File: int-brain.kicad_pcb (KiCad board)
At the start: 2 copper layers, 107 x 79.5 mm, 112 parts, among them J1 Top, J10 2MB, J11 1MB, J12 1MA, J13 1MA_ENC, J14 1MB_ENC, J15 2MA_ENC, J16 MPU9250, J17 VBATT_SELECT, J2 Bottom, J3 PWR, J4 PWR, J5 USB_A, J6 2MB_ENC, J7 I2C0, J8 UART0, J9 2MA, SW1 SW_Push, U1 PCA9635, U10 TPS5450DDA, U11 DRV8251ADDAR, U12 INA139, U13 AMS1117-3.3, U2 ESP32-DevKitC, U3 DRV8251ADDAR, U4 INA139, U5 DRV8251ADDAR, U6 INA139, U7 TPS5450DDA, U8 DRV8251ADDAR, U9 INA139

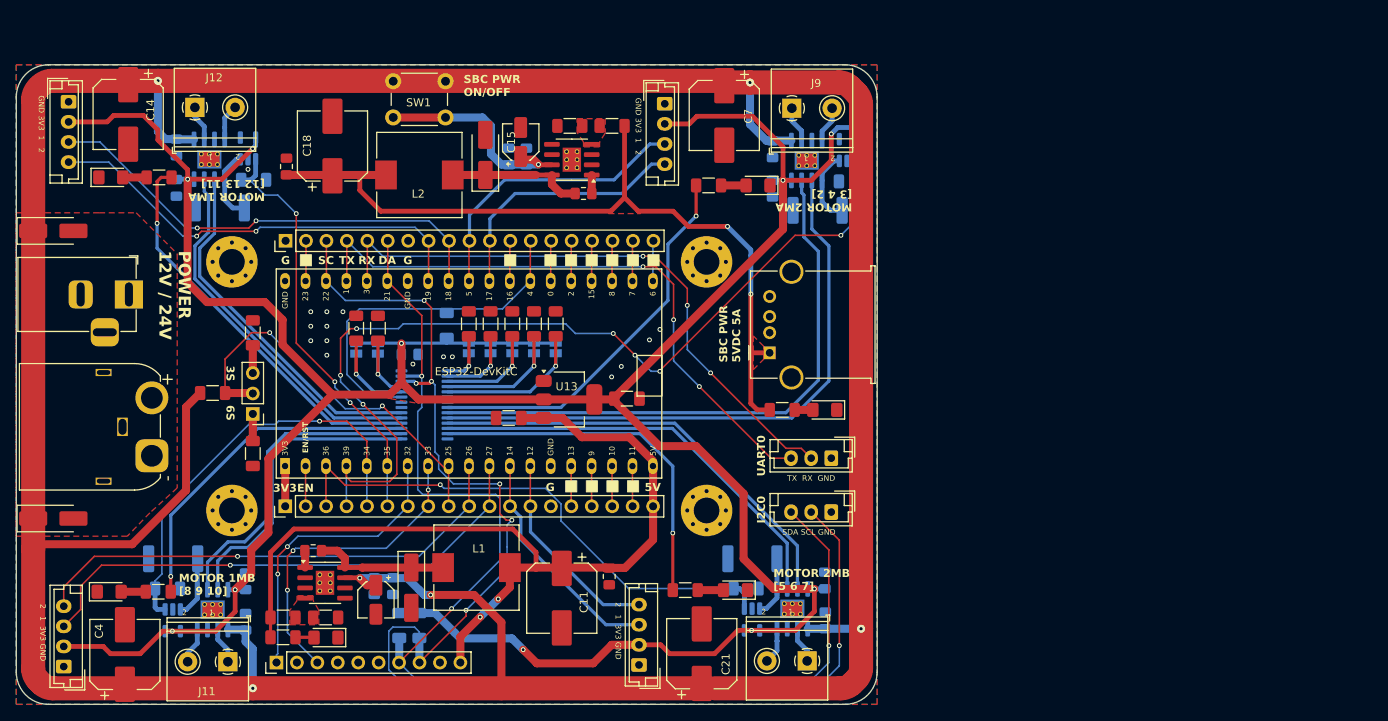
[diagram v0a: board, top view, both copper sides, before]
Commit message: change I2C and minor updates
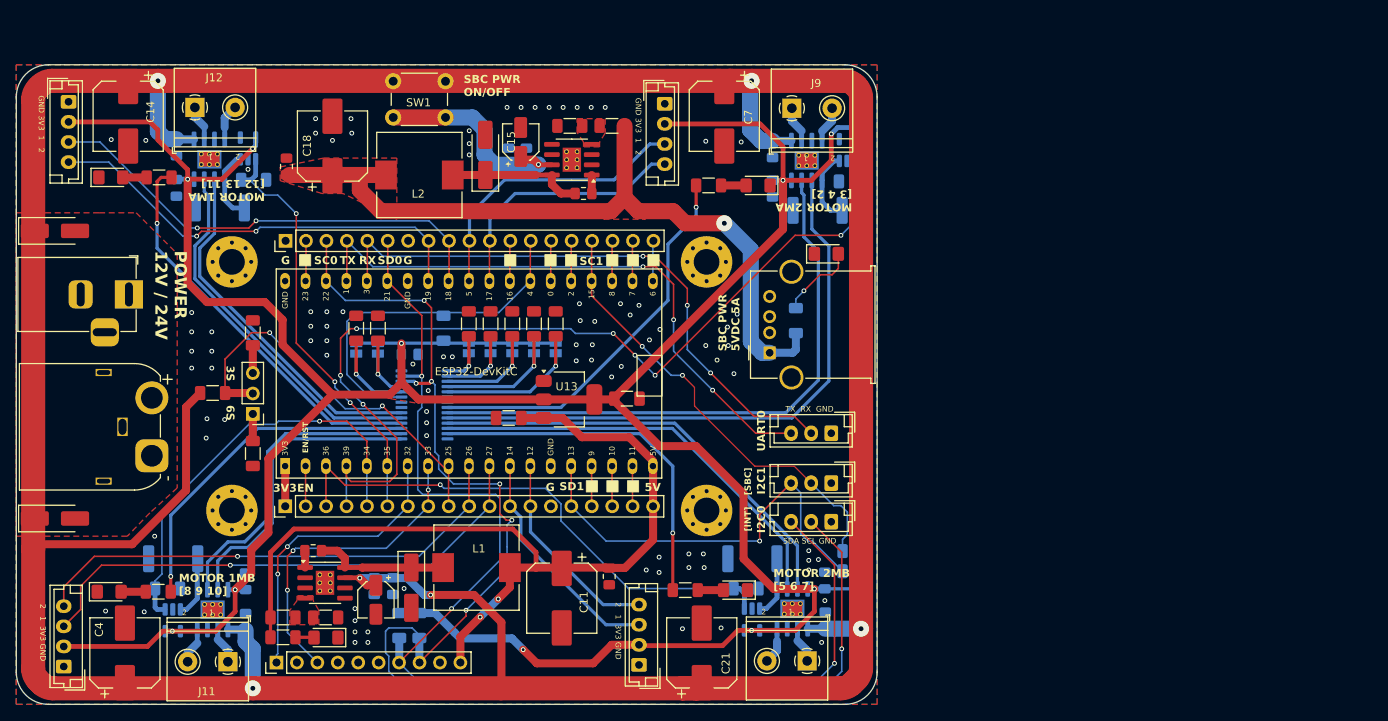
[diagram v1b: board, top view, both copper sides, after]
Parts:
- added J18: I2C0, Connector_JST:JST_EH_B3B-EH-A_1x03_P2.50mm_Vertical, F.Cu at (135.2, 124.5)
- added R32: 4.7k, Resistor_SMD:R_1206_3216Metric_Pad1.30x1.75mm_HandSolder, B.Cu at (138.2, 128.2)
- added R33: 4.7k, Resistor_SMD:R_1206_3216Metric_Pad1.30x1.75mm_HandSolder, B.Cu at (138.2, 130.7)
- J7: value I2C0 -> I2C1
- JP7: value I/O -> A6
- R13: moved to B.Cu
- SW1: value SW_Push -> ON/OFF
- moved D6 19.4 mm to (134.6, 91.2), turned to 0 degrees
- moved R13 11.2 mm to (130.8, 99.5), turned to 90 degrees
- moved J7 3.60 mm to (135.2, 119.7)
- moved J8 3.10 mm to (135.2, 113.5)
- moved R31 0.53 mm to (87.0, 100.5)
- moved C14 0.22 mm to (47.8, 74.1)
- moved D10 0.20 mm to (38.7, 124.1)
- moved D5 0.20 mm to (38.7, 88.3)
- moved C4 0.20 mm to (47.4, 140.8)
- moved C21 0.10 mm to (119.1, 140.8)
- moved C7 0.10 mm to (121.9, 74.1)
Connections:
- net /PCA_IO renamed /PCA_A6
- J1 pad 16: /GPIO15 -> /SCL1
- J2 pad 15: /GPIO13 -> /SDA1
- J7 pad 2: SCL0 -> /SCL1
- J7 pad 3: SDA0 -> /SDA1
- U2 pad 15: /GPIO13 -> /SDA1
- U2 pad 23: /GPIO15 -> /SCL1
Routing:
- net /SCL1: track 0.00 -> 56.2 mm, vias 0 -> 2
- net /SDA1: track 0.00 -> 52.9 mm, vias 0 -> 1
- net /PWR_LED_2: track 2.26 -> 9.81 mm, vias 0 -> 1
- net +3.3V: track 377.3 -> 383.9 mm
- net VS: track 456.3 -> 461.7 mm
- net /GPIO15: track 5.02 -> 0.00 mm
- net /GPIO13: track 5.01 -> 0.00 mm
- net /buck2/VOUT: track 100.2 -> 95.9 mm, vias 2 -> 1
- net /TX0: track 77.0 -> 75.0 mm
- net /RX0: track 75.8 -> 74.6 mm
- net GND: vias 16 -> 91
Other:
- board text added: "SC0"
- board text added: "SC1"
- board text added: "SD0"
- board text added: "SD1"
- board text added: "[INT]"
- board text added: "[SBC]"
- board text removed: "A0"
- board text removed: "A1"
- board text removed: "A2"
- board text removed: "A3"
- board text removed: "A4"
- board text removed: "A5"
- board text removed: "DA"
- board text removed: "I/O"
- board text removed: "SC"

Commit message: done?
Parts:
- JP1, JP2, JP3, JP4, JP5, JP6, JP7, R31: moved to F.Cu
- R11, R12, R14, R29, R4, R6, R7, R9: moved to B.Cu
- moved R14 27.7 mm to (57.7, 112.8), turned to 180 degrees
- moved D7 26.7 mm to (56.1, 117.8), turned to 90 degrees
- moved C26 19.5 mm to (114.6, 112.6), turned to 0 degrees
- moved D6 17.4 mm to (134.9, 108.6)
- moved U13 13.7 mm to (116.2, 107.4)
- moved C27 10.6 mm to (117.8, 102.2), turned to 180 degrees
- moved J18 5.40 mm to (135.2, 119.1)
- moved J7 5.10 mm to (135.2, 124.8)
- moved R27 3.70 mm to (121.7, 129.1)
- moved R31 3.35 mm to (86.9, 103.8), turned to 90 degrees
- moved R13 2.87 mm to (133.3, 100.9), turned to 0 degrees
- moved C9 1.22 mm to (80.9, 131.3), turned to 90 degrees
- moved C22 1.20 mm to (78.5, 131.3), turned to 90 degrees
- moved C25 0.11 mm to (67.5, 80.5)
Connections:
- J16 pad 10: VSS -> +3.3V
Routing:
- net SCL0: track 172.3 -> 126.2 mm, vias 7 -> 4
- net VS: track 461.7 -> 479.7 mm, vias 6 -> 5
- net /2MA_IN2: track 75.1 -> 60.5 mm
- net /2MA_IN1: track 73.5 -> 59.1 mm
- net /2MB_EN: track 45.1 -> 58.6 mm
- net VBATT: track 49.4 -> 36.5 mm, vias 2 -> 1
- net /SCL1: track 56.2 -> 68.7 mm, vias 2 -> 0
- net M_OE: track 44.4 -> 32.3 mm, vias 0 -> 2
- net /buck2/VOUT: track 95.9 -> 105.0 mm, vias 1 -> 0
- net /1MA2_ENC: track 54.7 -> 63.4 mm, vias 2 -> 1
- net SDA0: track 151.1 -> 142.4 mm, vias 3 -> 4
- net VSS: track 110.0 -> 101.7 mm, vias 2 -> 3
- net /1MA1_ENC: track 58.1 -> 66.1 mm, vias 2 -> 1
- net /SDA1: track 52.9 -> 45.0 mm
- net INT: track 39.8 -> 33.1 mm, vias 3 -> 0
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- removed copper zone on F.Cu, net +3.3V

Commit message: done
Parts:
- moved SW1 0.76 mm to (80.0, 69.6)
- moved C15 0.71 mm to (96.7, 78.0)
- moved C16 0.71 mm to (95.2, 79.8)
- moved C23 0.71 mm to (97.4, 79.8)
- moved R25 0.71 mm to (108.1, 76.0)
- moved C17 0.71 mm to (104.5, 84.4)
- moved C18 0.71 mm to (73.3, 78.5)
- moved C25 0.71 mm to (67.6, 81.2)
- moved R26 0.71 mm to (102.8, 76.0)
- moved U10 0.71 mm to (103.0, 80.2)
- moved D9 0.71 mm to (92.3, 79.6)
- moved L2 0.71 mm to (84.1, 82.1)
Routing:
- net VS: track 479.7 -> 476.5 mm
- net 2MA_SENSE: track 113.7 -> 114.7 mm
- net /buck2/BUCK_VIN: track 24.6 -> 25.6 mm
- net GND: vias 92 -> 107

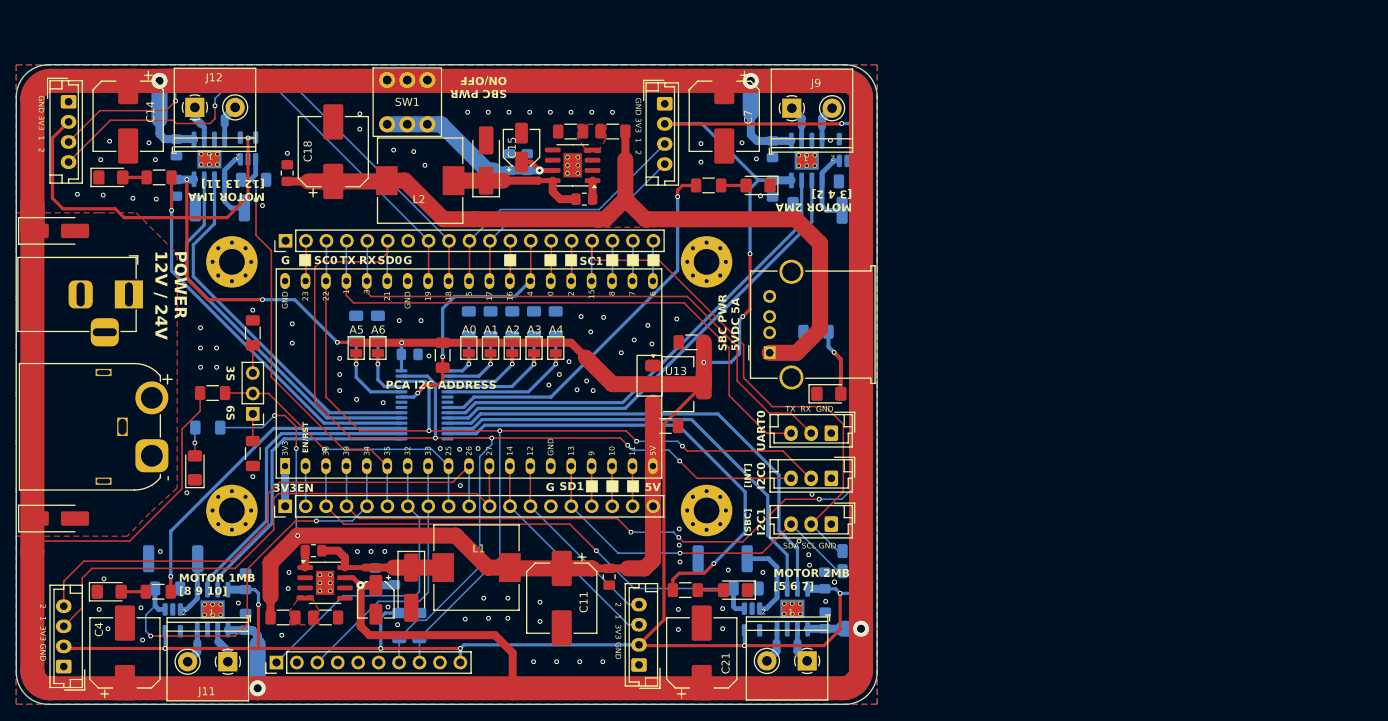
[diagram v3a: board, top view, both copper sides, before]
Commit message: basic redesign. PCB not up to date
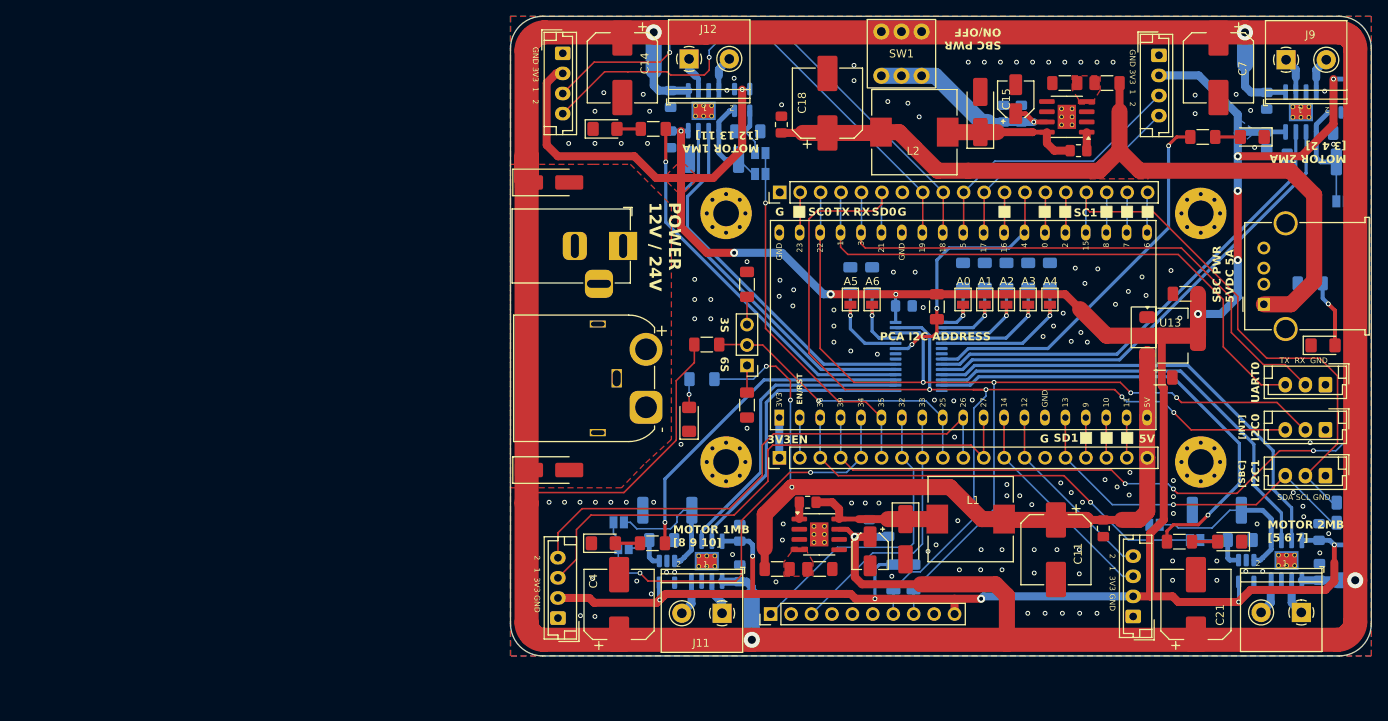
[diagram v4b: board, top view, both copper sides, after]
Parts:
- added JP10: PA, Jumper:SolderJumper-2_P1.3mm_Open_Pad1.0x1.5mm, B.Cu at (200.6, 79.5)
- added JP11: PA, Jumper:SolderJumper-2_P1.3mm_Open_Pad1.0x1.5mm, B.Cu at (180.4, 126.8)
- added JP12: SR, Jumper:SolderJumper-2_P1.3mm_Open_Pad1.0x1.5mm, B.Cu at (126.4, 81.3)
- added JP13: SR, Jumper:SolderJumper-2_P1.3mm_Open_Pad1.0x1.5mm, B.Cu at (108.8, 124.6)
- added JP14: SR, Jumper:SolderJumper-2_P1.3mm_Open_Pad1.0x1.5mm, B.Cu at (198.6, 84.7)
- added JP15: SR, Jumper:SolderJumper-2_P1.3mm_Open_Pad1.0x1.5mm, B.Cu at (175.4, 124.9)
- added JP8: PA, Jumper:SolderJumper-2_P1.3mm_Open_Pad1.0x1.5mm, B.Cu at (126.4, 78.7)
- added JP9: PA, Jumper:SolderJumper-2_P1.3mm_Open_Pad1.0x1.5mm, B.Cu at (109.4, 127.8)
- moved C10 61.7 mm to (132.3, 122.1)
- moved C17 61.7 mm to (165.9, 78.4)
- moved C20 61.7 mm to (195.9, 130.7)
- moved C21 61.7 mm to (180.5, 134.8)
- moved C22 61.7 mm to (139.9, 125.3)
- moved C25 61.7 mm to (129.0, 75.1)
- moved C26 61.7 mm to (176.0, 106.6)
- moved C8 61.7 mm to (140.0, 128.2)
- moved D3 61.7 mm to (187.5, 76.7)
- moved D8 61.7 mm to (144.4, 126.7)
- moved J10 61.7 mm to (193.6, 135.8)
- moved J13 61.7 mm to (175.9, 66.5)
- moved J16 61.7 mm to (127.7, 136.0)
- moved J18 61.7 mm to (196.6, 113.1)
- moved J7 61.7 mm to (196.6, 118.8)
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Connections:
- R18 pad 1: 1MB_SENSE -> Net-(JP9-A)
- R20 pad 1: 2MA_SENSE -> Net-(JP10-A)
- R24 pad 1: 1MA_SENSE -> Net-(JP8-A)
- R28 pad 1: 2MB_SENSE -> Net-(JP11-A)
- U12 pad 1: 2MB_SENSE -> Net-(JP11-A)
- U4 pad 1: 1MB_SENSE -> Net-(JP9-A)
- U6 pad 1: 2MA_SENSE -> Net-(JP10-A)
- U9 pad 1: 1MA_SENSE -> Net-(JP8-A)
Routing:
- net /motor-driver-4/IPROPI: track 10.7 -> 21.9 mm
- net /motor-driver-2/IPROPI: track 7.63 -> 17.8 mm
- net 1MA_SENSE: track 53.6 -> 45.9 mm
- net Net-(JP8-A): track 0.00 -> 7.21 mm
- net Net-(JP11-A): track 0.00 -> 7.10 mm
- net Net-(JP9-A): track 0.00 -> 6.55 mm
- net 2MB_SENSE: track 63.6 -> 57.1 mm
- net Net-(JP10-A): track 0.00 -> 6.19 mm
- net 2MA_SENSE: track 114.7 -> 108.6 mm
- net /motor-driver-3/IPROPI: track 9.60 -> 14.5 mm
- net +3.3V: track 387.3 -> 383.0 mm, vias 15 -> 16
- net /motor-driver-1/IPROPI: track 9.19 -> 12.0 mm
- net /2MB_IN1: track 59.9 -> 58.2 mm
- net 1MB_SENSE: track 50.6 -> 51.8 mm
- net VS: track 476.5 -> 477.1 mm
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- added copper zone on B.Cu, net +3.3V
- added copper zone on F.Cu, net +3.3V

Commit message: finally done?
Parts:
- added R34: R_TRIP, Resistor_SMD:R_1206_3216Metric_Pad1.30x1.75mm_HandSolder, B.Cu at (124.9, 70.9)
- added R35: R_TRIP, Resistor_SMD:R_1206_3216Metric_Pad1.30x1.75mm_HandSolder, B.Cu at (114.1, 132.0)
- added R36: R_TRIP, Resistor_SMD:R_1206_3216Metric_Pad1.30x1.75mm_HandSolder, B.Cu at (199.2, 71.0)
- added R37: R_TRIP, Resistor_SMD:R_1206_3216Metric_Pad1.30x1.75mm_HandSolder, B.Cu at (186.2, 131.9)
- JP10, JP11, JP8, JP9: value PA -> CA; moved to F.Cu
- JP12, JP13, JP14, JP15: moved to F.Cu
- R1, R2, R3, R5, R8: moved to B.Cu
- R14: value 470R -> 220R
- R17, R19, R23, R27: value 10mR -> R_SHUNT; moved to F.Cu
- R18, R20, R24, R28: value 24k -> R_GAIN
- moved J8 82.4 mm to (115.7, 92.3), turned to 90 degrees
- moved R32 42.9 mm to (168.4, 92.7)
- moved JP15 19.4 mm to (194.7, 123.0), turned to 90 degrees
- moved D6 17.5 mm to (196.4, 85.1)
- moved JP13 13.8 mm to (122.5, 123.2), turned to 90 degrees
- moved D7 12.4 mm to (116.9, 99.4), turned to -90 degrees
- moved JP11 12.2 mm to (192.0, 123.0), turned to -90 degrees
- moved JP9 11.4 mm to (119.8, 123.2), turned to -90 degrees
- moved JP12 10.0 mm to (116.4, 80.5), turned to -90 degrees
- moved JP14 8.89 mm to (190.7, 80.7), turned to -90 degrees
- moved JP8 7.49 mm to (119.1, 80.5), turned to 90 degrees
- moved JP10 7.32 mm to (193.4, 80.7), turned to 90 degrees
- moved R2 6.81 mm to (106.8, 124.2)
- moved C26 6.67 mm to (179.4, 112.3)
- moved R1 6.66 mm to (107.0, 78.4)
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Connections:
- JP10 pad 1: Net-(JP10-A) -> 2MA_SENSE
- JP10 pad 2: 2MA_SENSE -> /motor-driver-3/I_SEN_CA
- JP11 pad 1: Net-(JP11-A) -> 2MB_SENSE
- JP11 pad 2: 2MB_SENSE -> /motor-driver-4/I_SEN_CA
- JP12 pad 1: /motor-driver-1/IPROPI -> /motor-driver-1/I_SEN_SR
- JP13 pad 1: /motor-driver-2/IPROPI -> /motor-driver-2/I_SEN_SR
- JP14 pad 1: /motor-driver-3/IPROPI -> /motor-driver-3/I_SEN_SR
- JP15 pad 1: /motor-driver-4/IPROPI -> /motor-driver-4/I_SEN_SR
- JP8 pad 1: Net-(JP8-A) -> 1MA_SENSE
- JP8 pad 2: 1MA_SENSE -> /motor-driver-1/I_SEN_CA
- JP9 pad 1: Net-(JP9-A) -> 1MB_SENSE
- JP9 pad 2: 1MB_SENSE -> /motor-driver-2/I_SEN_CA
- R14 pad 1: VSS -> +3.3V
- R17 pad 2: GND -> /motor-driver-2/I_SEN_SR
- R18 pad 1: Net-(JP9-A) -> /motor-driver-2/I_SEN_CA
- R19 pad 2: GND -> /motor-driver-3/I_SEN_SR
- R20 pad 1: Net-(JP10-A) -> /motor-driver-3/I_SEN_CA
- R23 pad 2: GND -> /motor-driver-1/I_SEN_SR
- R24 pad 1: Net-(JP8-A) -> /motor-driver-1/I_SEN_CA
- R27 pad 2: GND -> /motor-driver-4/I_SEN_SR
- R28 pad 1: Net-(JP11-A) -> /motor-driver-4/I_SEN_CA
- U12 pad 1: Net-(JP11-A) -> /motor-driver-4/I_SEN_CA
- U12 pad 4: GND -> /motor-driver-4/I_SEN_SR
- U4 pad 1: Net-(JP9-A) -> /motor-driver-2/I_SEN_CA
- U4 pad 4: GND -> /motor-driver-2/I_SEN_SR
- U6 pad 1: Net-(JP10-A) -> /motor-driver-3/I_SEN_CA
- U6 pad 4: GND -> /motor-driver-3/I_SEN_SR
- U9 pad 1: Net-(JP8-A) -> /motor-driver-1/I_SEN_CA
- U9 pad 4: GND -> /motor-driver-1/I_SEN_SR
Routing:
- net VS: track 477.1 -> 423.8 mm, vias 5 -> 6
- net /TX0: track 72.7 -> 27.7 mm, vias 0 -> 1
- net /RX0: track 71.4 -> 29.7 mm, vias 0 -> 1
- net 2MA_SENSE: track 108.6 -> 77.4 mm, vias 3 -> 2
- net SDA0: track 142.4 -> 115.5 mm
- net VSS: track 101.6 -> 75.3 mm, vias 3 -> 0
- net 1MB_SENSE: track 51.8 -> 26.3 mm, vias 2 -> 0
- net /motor-driver-3/I_SEN_SR: track 0.00 -> 18.8 mm, vias 0 -> 1
- net /motor-driver-1/I_SEN_SR: track 0.00 -> 18.8 mm, vias 0 -> 1
- net /motor-driver-2/I_SEN_SR: track 0.00 -> 16.7 mm, vias 0 -> 1
- net /motor-driver-4/I_SEN_SR: track 0.00 -> 15.9 mm, vias 0 -> 1
- net 2MB_SENSE: track 57.1 -> 72.8 mm, vias 1 -> 2
- net /2MB_EN: track 58.6 -> 43.3 mm, vias 1 -> 0
- net GND: track 0.00 -> 14.3 mm, vias 139 -> 215
- net /SCL1: track 68.6 -> 55.2 mm, vias 0 -> 2
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- added copper zone on B.Cu, net /1MA1
- added copper zone on B.Cu, net /1MA2
- added copper zone on B.Cu, net /1MB1
- added copper zone on B.Cu, net /1MB2
- added copper zone on B.Cu, net /2MA1
- added copper zone on B.Cu, net /2MA2
- added copper zone on B.Cu, net /2MB1
- added copper zone on B.Cu, net /2MB2
- added copper zone on B.Cu, net VS
- added copper zone on F.Cu, net VSS
- removed copper zone on B.Cu, net +3.3V
- removed copper zone on F.Cu, net /buck2/VOUT
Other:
- outline, holes or cut-outs redrawn
- board text added: "107 mm x 79.5 mm"

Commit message: minor improvements
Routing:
- net VS: track 423.8 -> 428.8 mm
- net GND: vias 215 -> 235
- added copper zone on F.Cu, net /buck2/VOUT

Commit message: something
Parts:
- added C28: 10uF, Capacitor_SMD:C_1206_3216Metric_Pad1.33x1.80mm_HandSolder, B.Cu at (191.9, 95.9)
- added C29: 10uF, Capacitor_SMD:C_1206_3216Metric_Pad1.33x1.80mm_HandSolder, B.Cu at (172.9, 109.7)
- added C30: 10uF, Capacitor_SMD:C_1206_3216Metric_Pad1.33x1.80mm_HandSolder, B.Cu at (124.8, 112.3)
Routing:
- net VSS: track 75.3 -> 78.0 mm
- net +3.3VA: track 5.01 -> 7.38 mm
- net /buck2/VOUT: track 93.5 -> 94.6 mm
